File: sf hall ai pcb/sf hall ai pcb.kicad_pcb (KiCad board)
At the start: 2 copper layers, 73.4 x 48.4 mm, 13 parts, among them J1 Conn_01x06_Pin, U1 SS411A, U2 SS411A, U3 SS411A

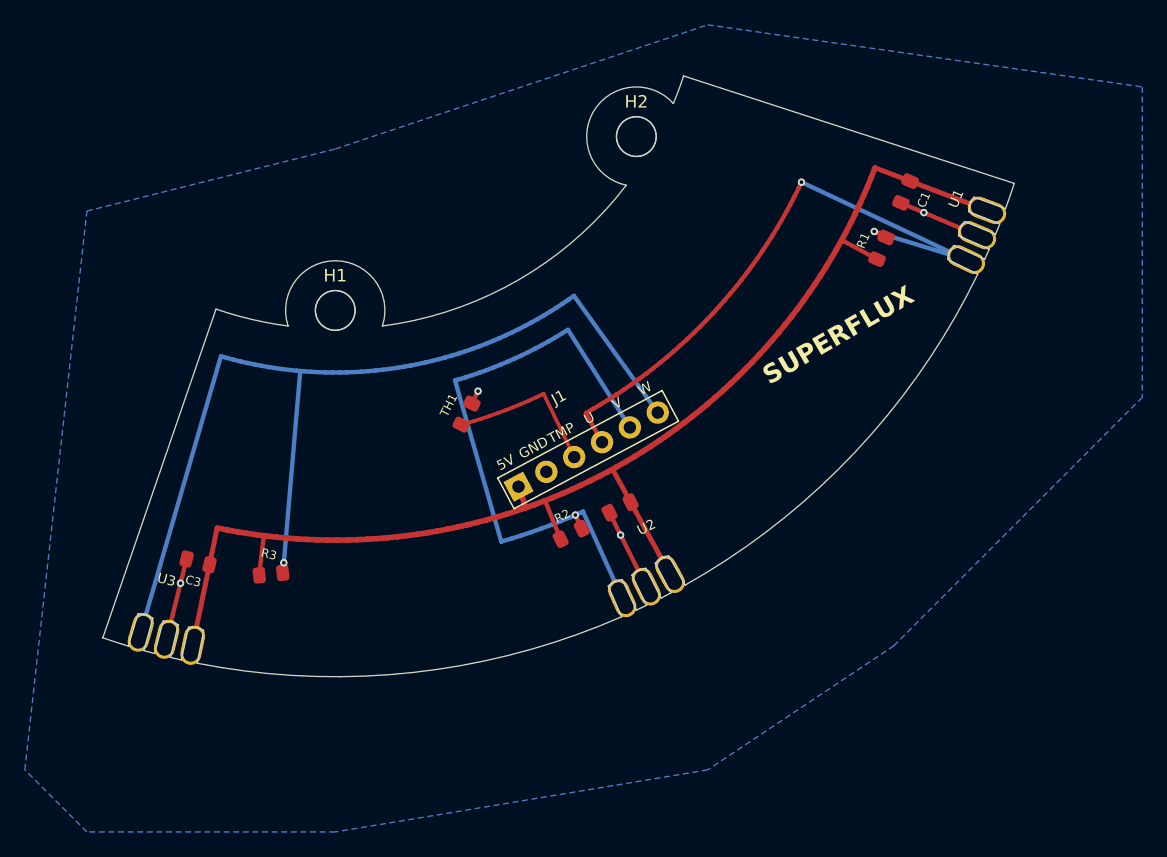
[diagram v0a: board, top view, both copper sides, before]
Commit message: feat: add new KiCad PCB designs and layouts for sf hall ai pcb and Q VFBMS32 AI PCB
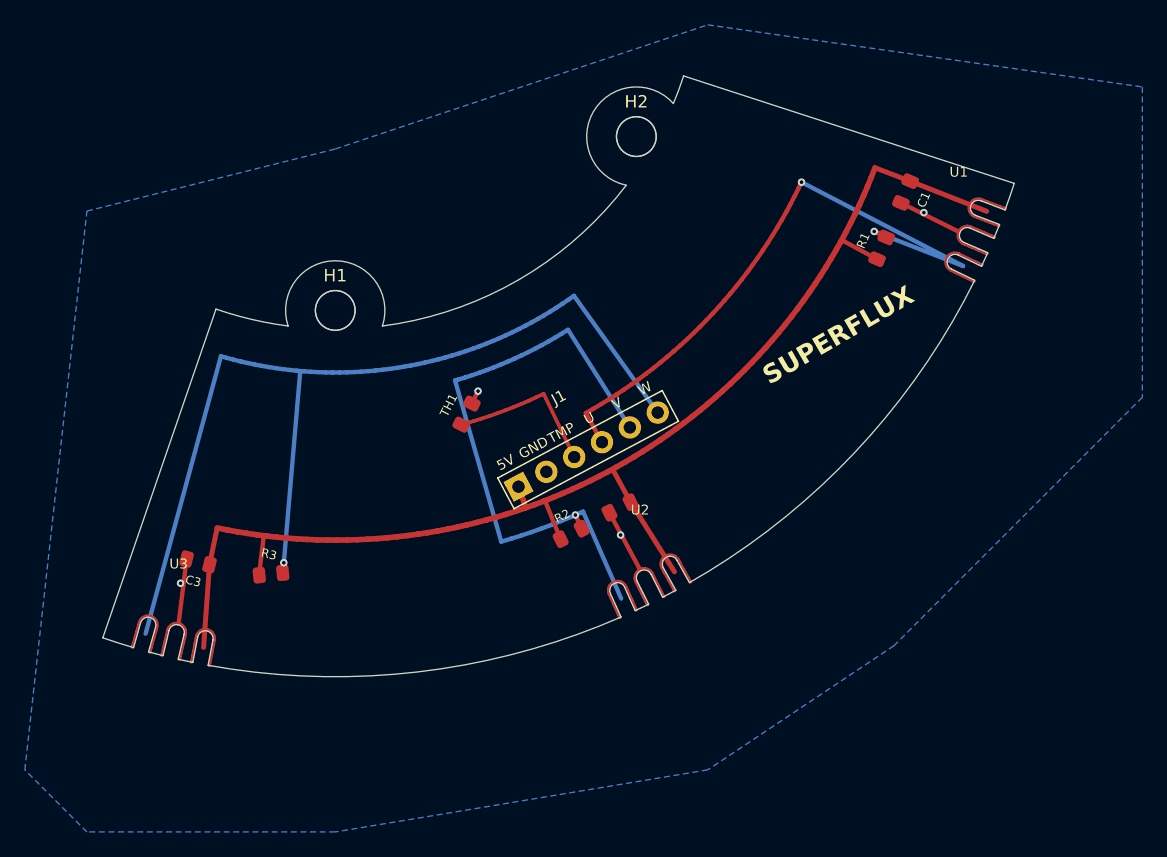
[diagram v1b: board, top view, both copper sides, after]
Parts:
- moved U3 1.60 mm to (-12.6, 53.2)
- moved U1 1.50 mm to (50.2, 21.7)
- moved U2 1.47 mm to (24.5, 48.9)
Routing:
- net GND: track 21.1 -> 16.8 mm
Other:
- outline, holes or cut-outs redrawn
- board text added: "TODO: Fix hall leg pads - need 3D edge plating in model"
